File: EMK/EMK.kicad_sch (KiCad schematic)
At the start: 53 parts, among them J1 USB_C_Receptacle_USB2.0_14P, J2 Conn_01x02_Socket, J3 Conn_ARM_JTAG_SWD_10, Q1 Si2371EDS, Q2 Si2371EDS, SW1 SW_Nidec_CAS-120A1, SW18 SW_Push, SW19 SW_Nidec_CAS-120A1, U1 nRF52840-QFAA, U2 15nH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

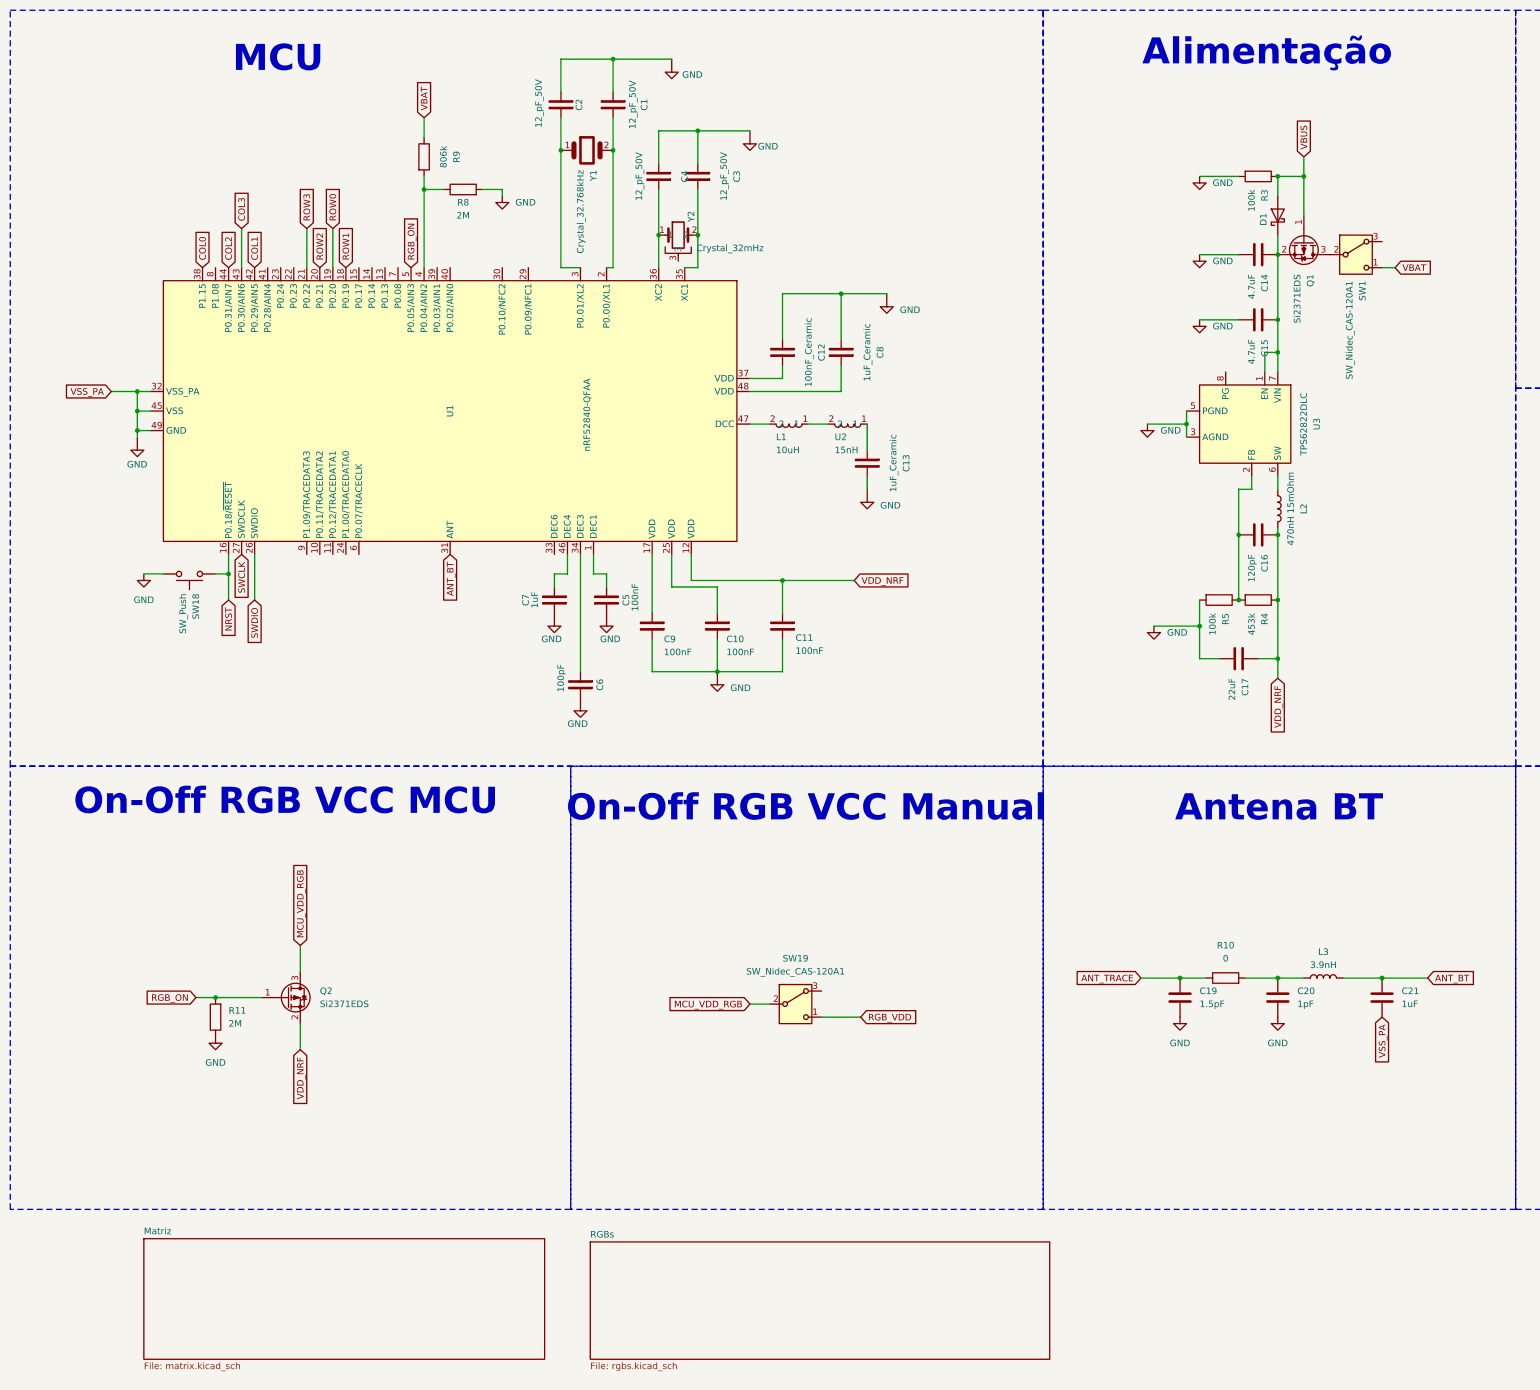
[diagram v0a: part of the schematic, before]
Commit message: feat: conclui a revisão 1 do EMK.
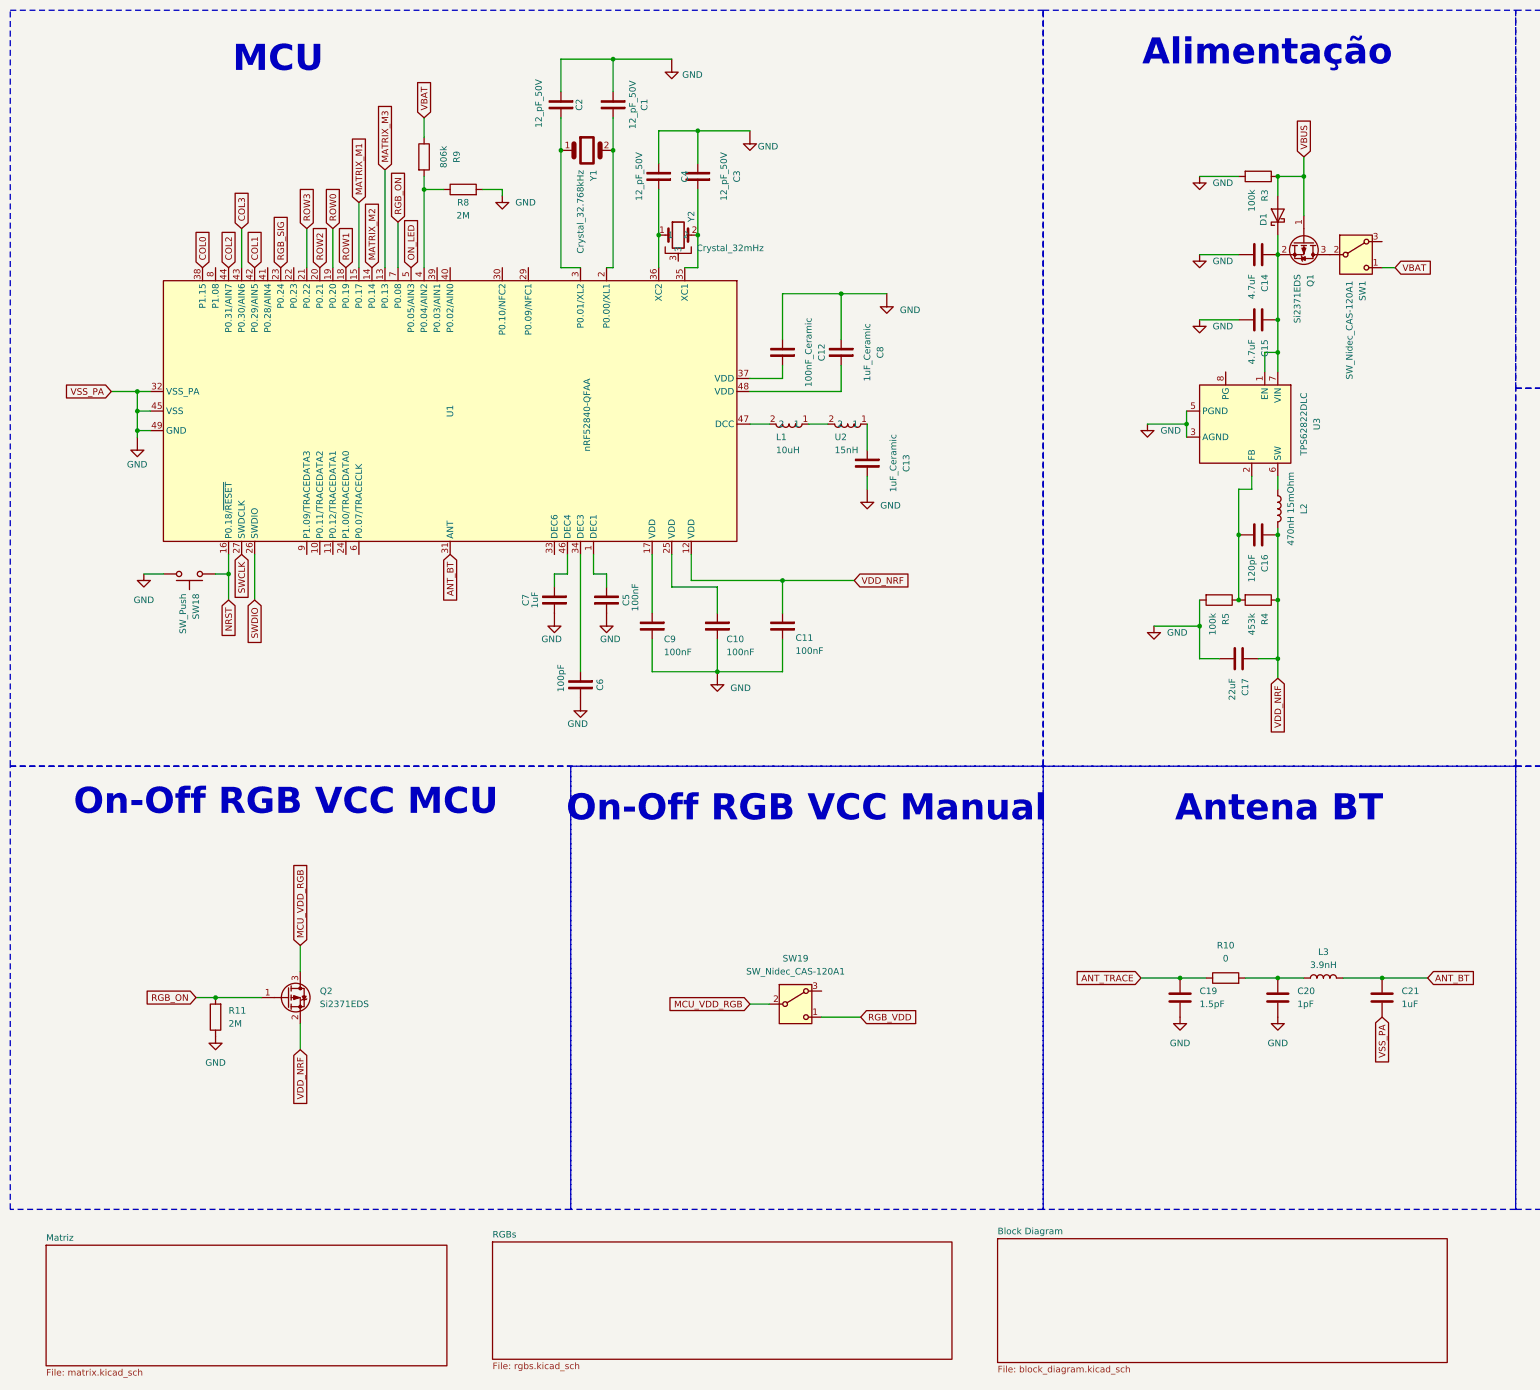
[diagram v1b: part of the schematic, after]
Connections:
- net RGB_ON: now also U1.7 (P0.08); no longer U1.5 (P0.05/AIN3)
- net MATRIX_M3: now reaches U1.13 (P0.13)
- net MATRIX_M2: now reaches U1.14 (P0.14)
- net MATRIX_M1: now reaches U1.15 (P0.17)
- net RGB_SIG: now reaches U1.23 (P0.24)
- new net ON_LED: U1.5 (P0.05/AIN3)
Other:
- added sheet Block Diagram (block_diagram.kicad_sch)
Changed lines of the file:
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@@
 	(wire
 		(pts
+			(xy 85.09 43.18) (xy 85.09 62.23)
+		)
+		(stroke
+			(width 0)
+			(type default)
+		)
+	)
+	(wire
+		(pts
 			(xy 355.6 109.22) (xy 344.17 109.22)
 		)
@@
 	(wire
 		(pts
+			(xy 87.63 53.34) (xy 87.63 62.23)
+		)
+		(stroke
+			(width 0)
+			(type default)
+		)
+	)
+	(wire
+		(pts
 			(xy 120.65 121.92) (xy 118.11 121.92)
 		)
@@
 	(wire
 		(pts
+			(xy 80.01 49.53) (xy 80.01 62.23)
+		)
+		(stroke
+			(width 0)
+			(type default)
+		)
+	)
+	(wire
+		(pts
 			(xy 119.38 62.23) (xy 123.19 62.23)
 		)
@@
 		)
 	)
+	(global_label "MATRIX_M2"
+		(shape input)
+		(at 82.55 62.23 90)
+		(fields_autoplaced yes)
+		(effects
+			(font
+				(size 1.27 1.27)
+			)
+			(justify left)
+		)
+		(property "Intersheetrefs" "${INTERSHEET_REFS}"
+			(at 82.55 49.0244 90)
+			(effects
+				(font
+					(size 1.27 1.27)
+				)
+				(justify left)
+				(hide yes)
+			)
+		)
+	)
 	(global_label "VBAT"
 		(shape input)
@@
 		)
 	)
+	(global_label "MATRIX_M1"
+		(shape input)
+		(at 80.01 49.53 90)
+		(fields_autoplaced yes)
+		(effects
+			(font
+				(size 1.27 1.27)
+			)
+			(justify left)
+		)
+		(property "Intersheetrefs" "${INTERSHEET_REFS}"
+			(at 80.01 36.3244 90)
+			(effects
+				(font
+					(size 1.27 1.27)
+				)
+				(justify left)
+				(hide yes)
+			)
+		)
+	)
 	(global_label "NRST"
 		(shape input)
@@
 		)
 	)
+	(global_label "RGB_SIG"
+		(shape input)
+		(at 64.77 62.23 90)
+		(fields_autoplaced yes)
+		(effects
+			(font
+				(size 1.27 1.27)
+			)
+			(justify left)
+		)
+		(property "Intersheetrefs" "${INTERSHEET_REFS}"
+			(at 64.77 51.3829 90)
+			(effects
+				(font
+					(size 1.27 1.27)
+				)
+				(justify left)
+				(hide yes)
+			)
+		)
+	)
 	(global_label "MCU_VDD_RGB"
 		(shape input)
@@
 		)
 	)
+	(global_label "MATRIX_M3"
+		(shape input)
+		(at 85.09 43.18 90)
+		(fields_autoplaced yes)
+		(effects
+			(font
+				(size 1.27 1.27)
+			)
+			(justify left)
+		)
+		(property "Intersheetrefs" "${INTERSHEET_REFS}"
+			(at 85.09 29.9744 90)
+			(effects
+				(font
+					(size 1.27 1.27)
+				)
+				(justify left)
+				(hide yes)
+			)
+		)
+	)
 	(global_label "RGB_ON"
 		(shape input)
@@
 	(global_label "RGB_ON"
 		(shape input)
-		(at 90.17 62.23 90)
+		(at 87.63 53.34 90)
 		(fields_autoplaced yes)
 		(effects
@@
 		)
 		(property "Intersheetrefs" "${INTERSHEET_REFS}"
-			(at 90.17 51.8062 90)
+			(at 87.63 42.9162 90)
 			(effects
 				(font
@@
 		)
 	)
+	(global_label "ON_LED"
+		(shape input)
+		(at 90.17 62.23 90)
+		(fields_autoplaced yes)
+		(effects
+			(font
+				(size 1.27 1.27)
+			)
+			(justify left)
+		)
+		(property "Intersheetrefs" "${INTERSHEET_REFS}"
+			(at 90.17 52.1691 90)
+			(effects
+				(font
+					(size 1.27 1.27)
+				)
+				(justify left)
+				(hide yes)
+			)
+		)
+	)
 	(global_label "SWDIO"
 		(shape input)
@@
 	)
 	(sheet
-		(at 125.095 252.095)
+		(at 106.045 252.095)
 		(size 89.535 22.86)
 		(fields_autoplaced yes)
@@
 		)
 		(property "Sheetname" "RGBs"
-			(at 125.095 251.3834 0)
+			(at 106.045 251.3834 0)
 			(effects
 				(font
@@
 		)
 		(property "Sheetfile" "rgbs.kicad_sch"
-			(at 125.095 275.5396 0)
+			(at 106.045 275.5396 0)
 			(effects
 				(font
@@
 	)
 	(sheet
-		(at 38.1 251.46)
+		(at 19.05 252.73)
 		(size 78.105 23.495)
 		(fields_autoplaced yes)
@@
 		)
 		(property "Sheetname" "Matriz"
-			(at 38.1 250.7484 0)
+			(at 19.05 252.0184 0)
 			(effects
 				(font
@@
 		)
 		(property "Sheetfile" "matrix.kicad_sch"
-			(at 38.1 275.5396 0)
+			(at 19.05 276.8096 0)
 			(effects
 				(font
@@
 				)
 			)
+		)
+	)
+	(sheet
+		(at 204.47 251.46)
+		(size 87.63 24.13)
+		(fields_autoplaced yes)
+		(stroke
+			(width 0.1524)
+			(type solid)
+		)
+		(fill
+			(color 0 0 0 0.0000)
+		)
+		(property "Sheetname" "Block Diagram"
+			(at 204.47 250.7484 0)
+			(effects
+				(font
+					(size 1.27 1.27)
+				)
+				(justify left bottom)
+			)
+		)
+		(property "Sheetfile" "block_diagram.kicad_sch"
+			(at 204.47 276.1746 0)
+			(effects
+				(font
+					(size 1.27 1.27)
+				)
+				(justify left top)
+			)
+		)
+		(instances
+			(project "EMK"
+				(path "/b49e0e20-ddc2-4eb4-9509-7721d6b2744b"
+					(page "4")
+				)
+			)
